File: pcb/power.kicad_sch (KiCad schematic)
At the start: 30 parts, among them U3 TLV75533PDBVR, U4 BQ24078RGTR

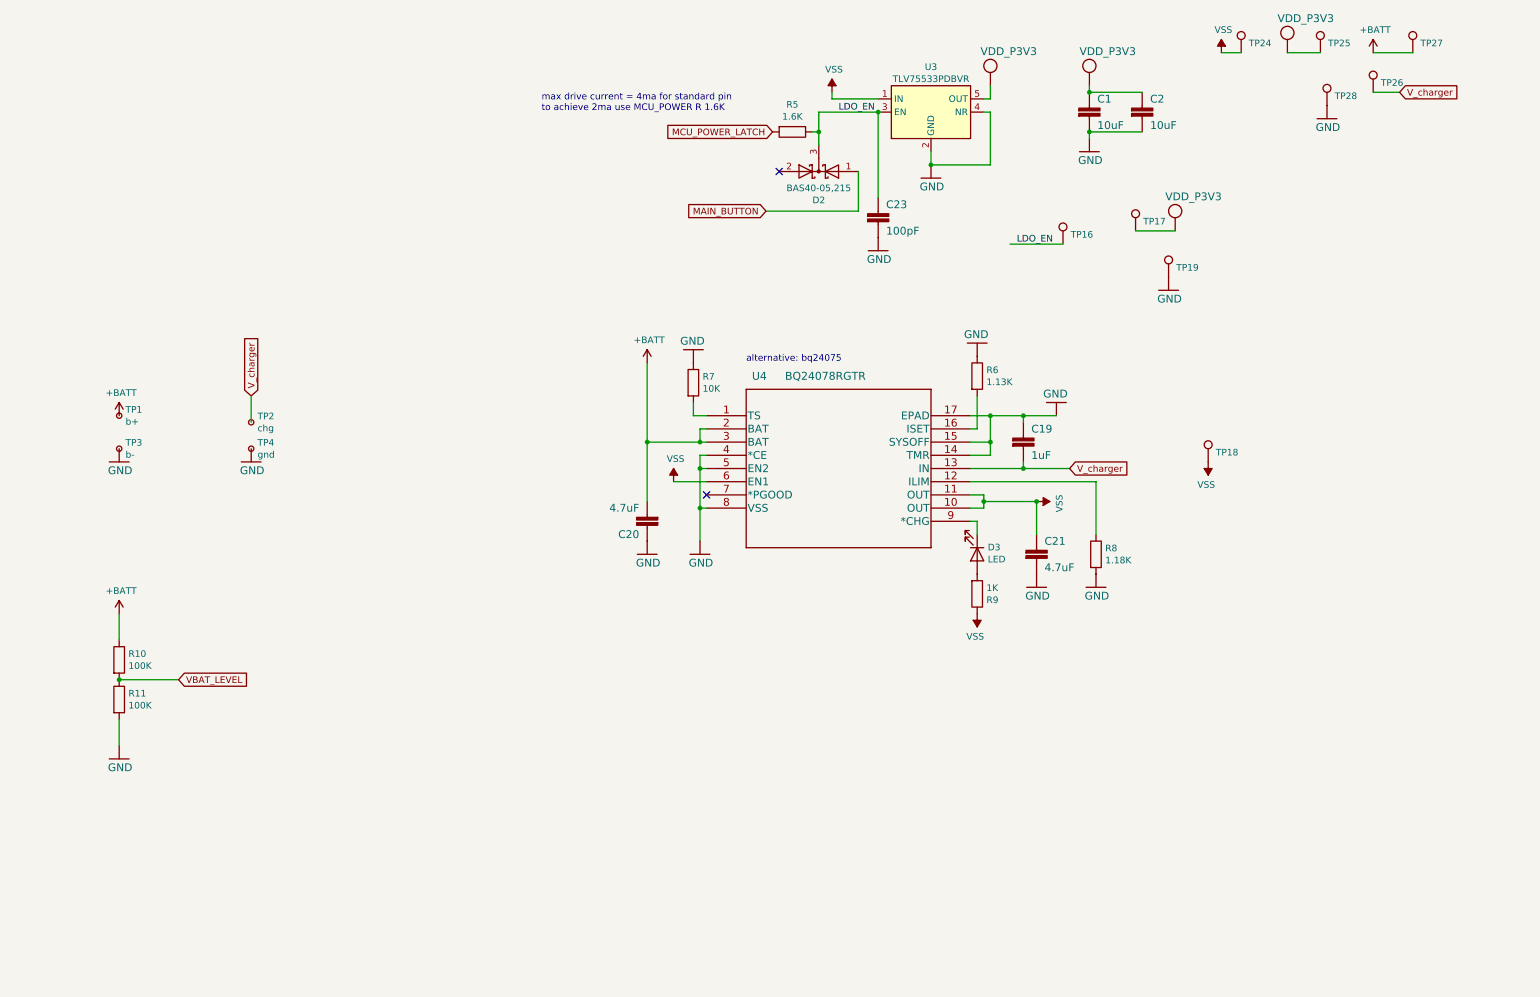
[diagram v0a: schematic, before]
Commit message: [pcb] version 1.3 (#75)
Changes:
    LDO voltage regulator replaced with DC-DC (expected increase in efficiency)
    added small-footprint RTC chip
    analog latch for regulator EN pin replaced with a digital flip-flop

Fixture:
    added Raspberry Pico to the PCB
    added current measurement setup
    planning to reduce hardware in use to a single PCB
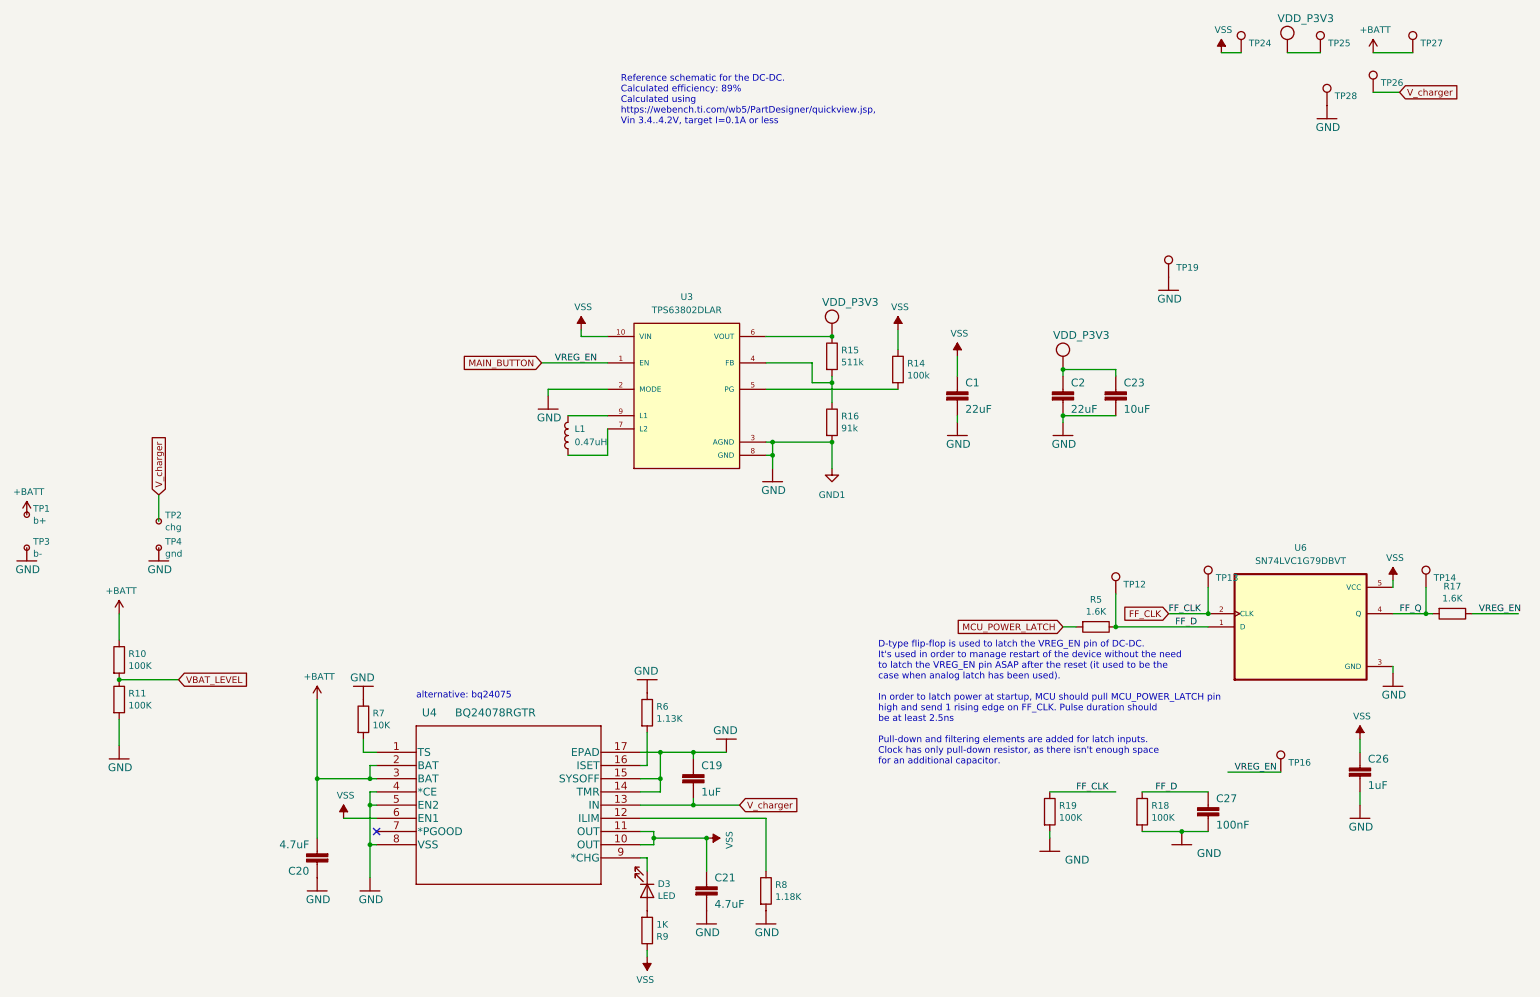
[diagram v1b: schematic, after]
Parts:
- removed D2: BAS40-05,215, Package_TO_SOT_SMD:SOT-23, symbol nRF52832_qfaa-rescue:D_Schottky_x2_KCom_AAK-Device
- removed TP17, TP18: TestPoint, TestPoint:TestPoint_Pad_D1.0mm, symbol Connector:TestPoint
- removed U3: TLV75533PDBVR, Package_TO_SOT_SMD:SOT-23-5, symbol Regulator_Linear:TPS73133DBV
- added C26: 1uF, Capacitor_SMD:C_0402_1005Metric, symbol nRF52832_qfaa-eagle-import:CAPACITOR_0402_N
- added C27: 100nF, Capacitor_SMD:C_0402_1005Metric, symbol nRF52832_qfaa-eagle-import:CAPACITOR_0402_N
- added L1: 0.47uH, Inductor_SMD:L_1008_2520Metric, symbol Device:L
- added R14: 100k, Resistor_SMD:R_0402_1005Metric, symbol Device:R
- added R15: 511k, Resistor_SMD:R_0402_1005Metric, symbol Device:R
- added R16: 91k, Resistor_SMD:R_0402_1005Metric, symbol Device:R
- added R17: 1.6K, Resistor_SMD:R_0402_1005Metric, symbol Device:R
- added R18, R19: 100K, Resistor_SMD:R_0402_1005Metric, symbol Device:R
- added TP12, TP13, TP14: TestPoint, TestPoint:TestPoint_Pad_D1.0mm, symbol Connector:TestPoint
- added U3: TPS63802DLAR, VREG_TPS63802DLAR, symbol custom:TPS63802DLAR
- added U6: SN74LVC1G79DBVT, Package_TO_SOT_SMD:SOT-23-5, symbol custom:SN74LVC1G79DBVT
- C1, C2: value 10uF -> 22uF; footprint Capacitor_SMD:C_0402_1005Metric -> Capacitor_SMD:C_0603_1608Metric; LCSC C15525 -> C109447
- C23: value 100pF -> 10uF; LCSC C1546 -> C15525
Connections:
- net GND: now also C26.2, C27.2, R16.2, R18.2, R19.2, U3.2 (MODE), U3.3 (AGND), U3.8 (GND), U6.3 (GND)
- net MAIN_BUTTON: now also TP16.1, R17.1, U3.1 (EN)
- net VCC: now also C23.1, R15.1, U3.6 (VOUT); no longer C1.1
- net VSS: now also C1.1, C26.1, R14.1, U3.10 (VIN), U6.5 (VCC)
- removed net LDO_EN: C23.1, R5.1, TP16.1
- new net: R15.2, R16.1, U3.4 (FB)
- new net: R14.2, U3.5 (PG)
- new net: L1.1, U3.7 (L2)
- new net: L1.2, U3.9 (L1)
- new net FF_CLK: R19.1, TP13.1, U6.2 (CLK)
- new net FF_D: C27.1, R18.1, R5.1, TP12.1, U6.1 (D)
- new net FF_Q: R17.2, TP14.1, U6.4 (Q)
- no-connect marks 2 -> 1
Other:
- note added: "D-type flip-flop is used to latch the VREG_EN pin of DC-DC. It's used in order to manage restart of the device without the need to latch the VREG_EN pin ASAP after the reset (it used to be the case when analog latch has been used). In order to latch power at startup, MCU should pull MCU_POWER_LATCH pin high and send 1 rising edge on FF_CLK. Pulse duration should be at least 2.5ns Pull-down and fi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"
- note added: "Reference schematic for the DC-DC. Calculated efficiency: 89% Calculated using https://webench.ti.com/wb5/PartDesigner/quickview.jsp, Vin 3.4..4.2V, target I=0.1A or less"
- note removed: "max drive current = 4ma for standard pin to achieve 2ma use MCU_POWER R 1.6K"
- moved on the sheet: C19, C20, C21, D3, R6, R7, R8, R9, TP1, TP16, TP2, TP3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

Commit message: PCB v1.4 (#175)
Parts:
- removed TP1: b+, TestPoint:TestPoint_Pad_D1.0mm, symbol Connector:TestPoint_Small
- removed TP3: b-, TestPoint:TestPoint_Pad_D1.0mm, symbol Connector:TestPoint_Small
- added J4: Conn_01x02_Socket, _other:SM02B-SRSS-TB_LF__SN_, symbol Connector:Conn_01x02_Socket
- C19, C26: LCSC C52923 -> C77007
- D3: LCSC C72043 -> C131282
- R10, R11: value 100K -> 1M; LCSC C25741 -> C226699
- R14: value 100k -> 100K
- R15: value 511k -> 255k; footprint Resistor_SMD:R_0402_1005Metric -> Resistor_SMD:R_0603_1608Metric; LCSC C144750 -> C728604
- R16: footprint Resistor_SMD:R_0402_1005Metric -> Resistor_SMD:R_0603_1608Metric; LCSC C4190 -> C227535
- U3: footprint VREG_TPS63802DLAR -> df_components:VREG_TPS63802DLAR
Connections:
- net +BATT: now also J4.2 (Pin_2)
- net GND: now also J4.1 (Pin_1)
- net VCC: now also R15.2; no longer R15.1
- net at R16.1, U3.4 (FB): now also R15.1; no longer R15.2
- net MAIN_BUTTON renamed VREG_EN
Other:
- note added: "Reference schematic for the DC-DC. Calculated efficiency: 92% Calculated using https://webench.ti.com/wb5/PartDesigner/quickview.jsp, Vin 2.5..5.5V, target I=0.1A or less"
- note removed: "Reference schematic for the DC-DC. Calculated efficiency: 89% Calculated using https://webench.ti.com/wb5/PartDesigner/quickview.jsp, Vin 3.4..4.2V, target I=0.1A or less"
- moved on the sheet: R15, TP24, TP25, TP26, TP27, TP28
